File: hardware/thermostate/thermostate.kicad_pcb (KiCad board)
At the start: 4 copper layers, 80 x 80 mm, 44 parts, among them IC1 L8050QLT1G, IC2 L8050QLT1G, J1 Conn_01x02_Male, J2 Conn_01x02_Male, K1 SRD-03VDC-SL-C, P1 USB_C_Plug_USB2.0, Q1 BC847, Q2 BC847, SW1 SW_Push, SW2 SW_Push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

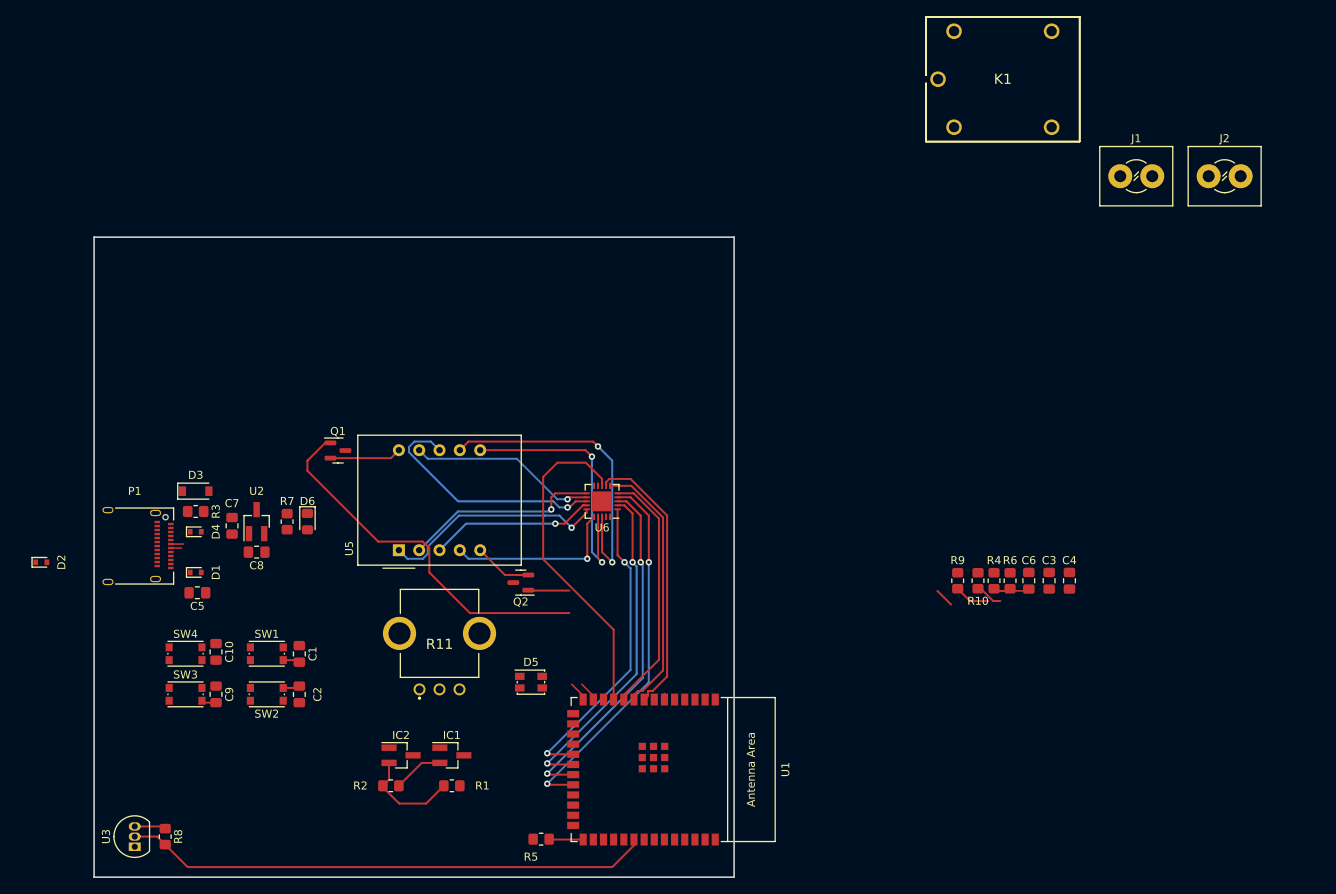
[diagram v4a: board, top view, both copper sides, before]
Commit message: Add SCH with low power components
Signed-off-by: Javier <javierfernandezvillasante@gmail.com>
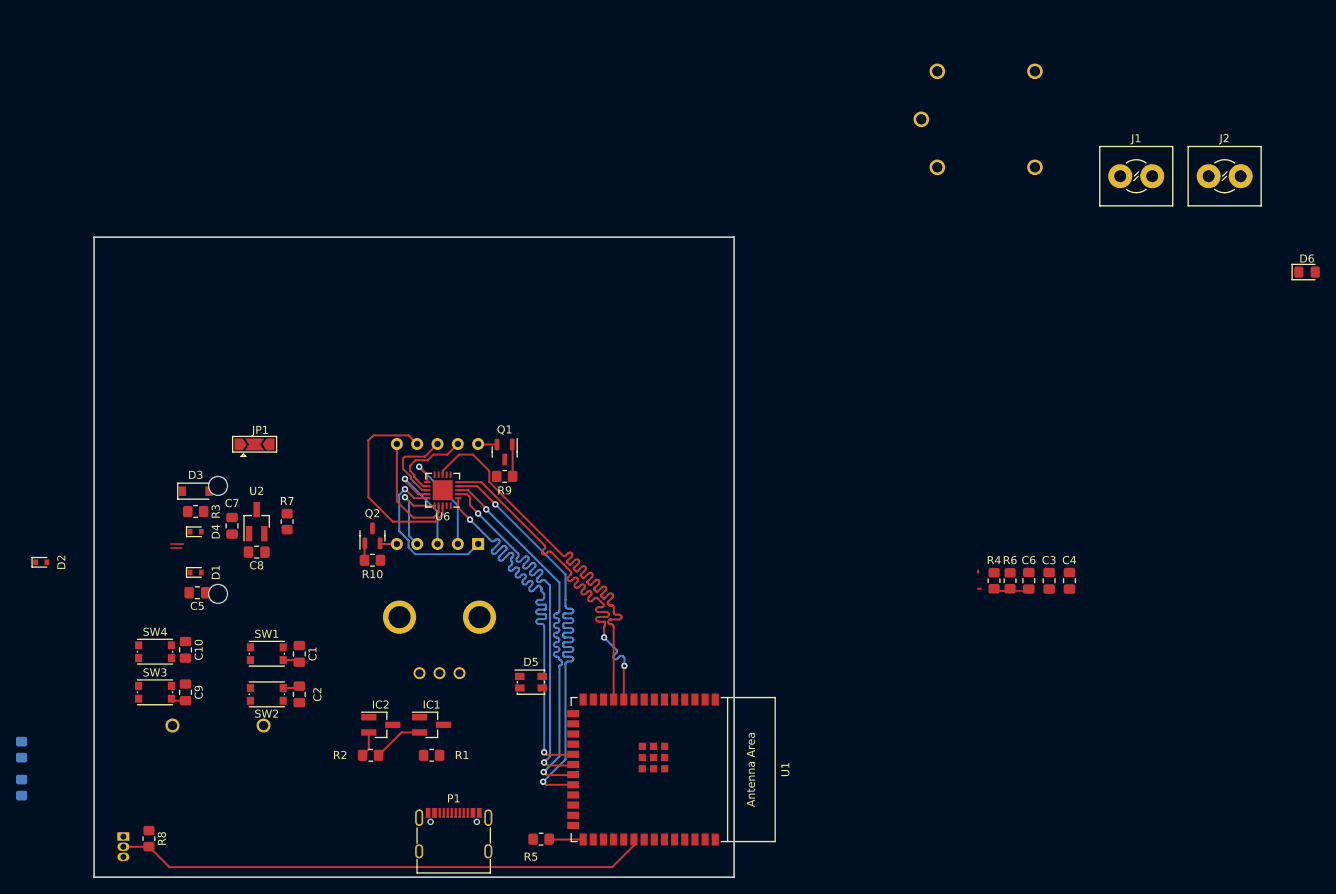
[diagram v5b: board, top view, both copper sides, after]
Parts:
- added BT1: BC2AAAPC, BC2AAAPC:BAT_BC2AAAPC, B.Cu at (122.2, 91.2)
- added JP1: Jumper_3_Bridged12, Jumper:SolderJumper-3_P2.0mm_Open_TrianglePad1.0x1.5mm, F.Cu at (126.7, 79.2)
- added R10: 10k (1%), Resistor_SMD:R_0805_2012Metric_Pad1.20x1.40mm_HandSolder, B.Cu at (97.6, 117.4)
- added R9: 10k (1%), Resistor_SMD:R_0805_2012Metric_Pad1.20x1.40mm_HandSolder, B.Cu at (97.6, 122.1)
- K1, R11, U3, U5: moved to B.Cu
- P1: footprint Connector_USB:USB_C_Receptacle_Amphenol_12401610E4-2A -> Connector_USB:USB_C_Receptacle_G-Switch_GT-USB-7010ASV
- moved D6 128.8 mm to (258.3, 57.7), turned to 0 degrees
- moved R10 75.7 mm to (141.5, 93.7), turned to 180 degrees
- moved R9 58.1 mm to (158.0, 83.2), turned to 0 degrees
- moved P1 54.8 mm to (151.6, 129.0), turned to 0 degrees
- moved Q1 20.8 mm to (158.0, 80.2), turned to -90 degrees
- moved U6 20.0 mm to (150.3, 85.0)
- moved Q2 19.4 mm to (141.5, 90.7), turned to 90 degrees
- moved U5 9.94 mm to (154.7, 91.7)
- moved K1 7.29 mm to (212.1, 32.6)
- moved IC1 4.57 mm to (148.9, 114.3)
- moved IC2 4.57 mm to (142.5, 114.3)
- moved R1 4.57 mm to (148.9, 118.1)
- moved R2 4.57 mm to (141.2, 118.1)
- moved C10 3.82 mm to (118.1, 104.9)
- moved C9 3.82 mm to (118.1, 110.2)
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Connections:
- C7 pad 1: +5V -> Net-(C7-Pad1)
- U2 pad 3: +5V -> Net-(C7-Pad1)
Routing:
- net Net-(Q1-Pad1): track 47.0 -> 4.01 mm
- net 7SEG_G: track 34.7 -> 0.00 mm
- net 7SEG_F: track 32.9 -> 0.58 mm
- net 7SEG_A: track 38.8 -> 58.8 mm
- net Net-(U5-Pad8): track 30.6 -> 10.6 mm, vias 1 -> 0
- net Net-(U5-Pad6): track 33.9 -> 14.3 mm, vias 2 -> 0
- net 7SEG_DP: track 41.3 -> 59.7 mm
- net 7SEG_E: track 33.6 -> 50.6 mm, vias 0 -> 2
- net 7SEG_D: track 46.9 -> 61.6 mm
- net Net-(U5-Pad7): track 39.4 -> 25.9 mm, vias 2 -> 0
- net Net-(U5-Pad9): track 23.6 -> 10.8 mm, vias 1 -> 0
- net Net-(U5-Pad4): track 22.0 -> 10.6 mm
- net Net-(U5-Pad2): track 24.8 -> 14.0 mm
- net DTR: track 12.7 -> 3.36 mm
- net 7SEG_B: track 41.7 -> 50.6 mm
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
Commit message: New PCB desing
Signed-off-by: Javier <javierfernandezvillasante@gmail.com>
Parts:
- added D7: 1N4148W, Diode_SMD:D_SOD-123, F.Cu at (171.1, 86.0)
- added P2: 1929517, phoenix_terminalBlock:PHOENIX_1929517, B.Cu at (145.3, 63.8)
- added U4: IRLML2502TRPBF, Package_TO_SOT_SMD:SOT-23, F.Cu at (171.1, 89.3)
- R10, R9: moved to F.Cu
- moved R10 130.0 mm to (220.1, 73.9), turned to 0 degrees
- moved R9 127.3 mm to (215.4, 73.9), turned to 0 degrees
- moved SW2 58.7 mm to (183.4, 90.4), turned to -90 degrees
- moved C5 57.1 mm to (62.5, 99.3)
- moved D3 56.9 mm to (62.5, 85.9)
- moved C2 56.5 mm to (183.4, 86.4), turned to 180 degrees
- moved C10 54.1 mm to (64.0, 106.2)
- moved C7 54.1 mm to (69.8, 90.7)
- moved C8 54.1 mm to (72.9, 94.0)
- moved C9 54.1 mm to (64.0, 111.5)
- moved R7 54.1 mm to (76.7, 90.2)
- moved U2 54.1 mm to (72.9, 90.2)
- moved SW3 54.1 mm to (60.2, 111.5)
- moved SW4 54.1 mm to (60.2, 106.4)
- moved D1 54.1 mm to (65.3, 96.5)
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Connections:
- K1 pad 4: unconnected-(K1-Pad4) -> Net-(D7-Pad1)
- K1 pad 5: unconnected-(K1-Pad5) -> GND
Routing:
- net Net-(IC2-Pad3): track 0.00 -> 45.7 mm, vias 0 -> 2
- net /ESP32_minimal/USB_N: track 1.80 -> 47.2 mm
- net /ESP32_minimal/USB_P: track 2.05 -> 45.9 mm
- net Net-(D7-Pad1): track 0.00 -> 42.5 mm
- net AC: track 0.00 -> 28.9 mm
- net GND1: track 0.00 -> 26.4 mm
- net GPIO38: track 0.00 -> 23.2 mm
- net ESP_3V3: track 0.00 -> 6.05 mm
- net DTR: track 3.36 -> 8.84 mm
- net CHIP_PU: track 2.11 -> 6.81 mm
- net GND: track 0.00 -> 1.93 mm
- net RTS: track 6.30 -> 4.38 mm
- net VBUS: track 0.00 -> 0.62 mm

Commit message: Stop until next winter
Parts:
- removed the R10 at (220.1, 73.9)
- removed the R10 at (141.5, 93.7)
- removed the R9 at (215.4, 73.9)
- removed the R9 at (158.0, 83.2)
- added R10: 10k (1%), Resistor_SMD:R_0805_2012Metric_Pad1.20x1.40mm_HandSolder, F.Cu at (144.1, 101.1)
- added R9: 10k (1%), Resistor_SMD:R_0805_2012Metric_Pad1.20x1.40mm_HandSolder, F.Cu at (164.5, 95.2)
- K1, P2, U3: moved to F.Cu
- moved D5 231.2 mm to (385.6, 68.9), turned to 0 degrees
- moved IC2 202.1 mm to (376.6, 68.9)
- moved IC1 197.7 mm to (377.6, 62.9)
- moved R5 197.3 mm to (348.6, 62.9), turned to 0 degrees
- moved R4 192.1 mm to (362.6, 63.9), turned to 0 degrees
- moved R1 191.5 mm to (369.6, 58.9)
- moved R2 182.6 mm to (354.6, 58.9), turned to 0 degrees
- moved SW1 176.4 mm to (349.6, 132.9), turned to 0 degrees
- moved R6 171.7 mm to (344.6, 67.9), turned to 0 degrees
- moved C2 171.3 mm to (349.6, 127.9), turned to 0 degrees
- moved SW2 164.2 mm to (342.6, 130.9), turned to 0 degrees
- moved J1 152.5 mm to (113.3, 137.7)
- moved J2 152.1 mm to (124.7, 137.5)
- moved C6 152.0 mm to (329.6, 130.9), turned to 0 degrees
- moved R7 136.4 mm to (210.7, 115.8), turned to 90 degrees
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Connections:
- U1 pad 16: unconnected-(U1-Pad16) -> RelayControlSignal
- U1 pad 18: unconnected-(U1-Pad18) -> Potenciometro
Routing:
- net BatterySupply: track 0.00 -> 117.5 mm, vias 0 -> 1
- net RelayControlSignal: track 0.00 -> 110.3 mm, vias 0 -> 2
- net ExternalPush_1: track 1.86 -> 98.9 mm, vias 0 -> 2
- net ExternalPush_2: track 0.00 -> 93.4 mm, vias 0 -> 2
- net 7SEG_F: track 0.58 -> 84.5 mm
- net 7SEG_G: track 0.00 -> 77.8 mm
- net Potenciometro: track 0.00 -> 55.3 mm, vias 0 -> 4
- net 7SEG_A: track 58.8 -> 106.5 mm
- net 7SEG_B: track 50.6 -> 96.9 mm
- net Net-(IC2-Pad3): track 45.7 -> 0.00 mm, vias 2 -> 0
- net TemperatureSensor: track 66.7 -> 106.6 mm, vias 0 -> 2
- net Net-(D7-Pad1): track 42.5 -> 3.90 mm
- net 7SEG_E: track 50.6 -> 84.6 mm, vias 2 -> 0
- net +5V: track 0.00 -> 28.7 mm
- net GPIO38: track 23.2 -> 0.00 mm
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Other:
- board size 80 x 80 mm -> 119.2 x 79.2 mm
